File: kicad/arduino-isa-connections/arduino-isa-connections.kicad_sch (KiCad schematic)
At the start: 2 parts, among them J1 Trident TVGA9000i-1, X1 14.31818MHz

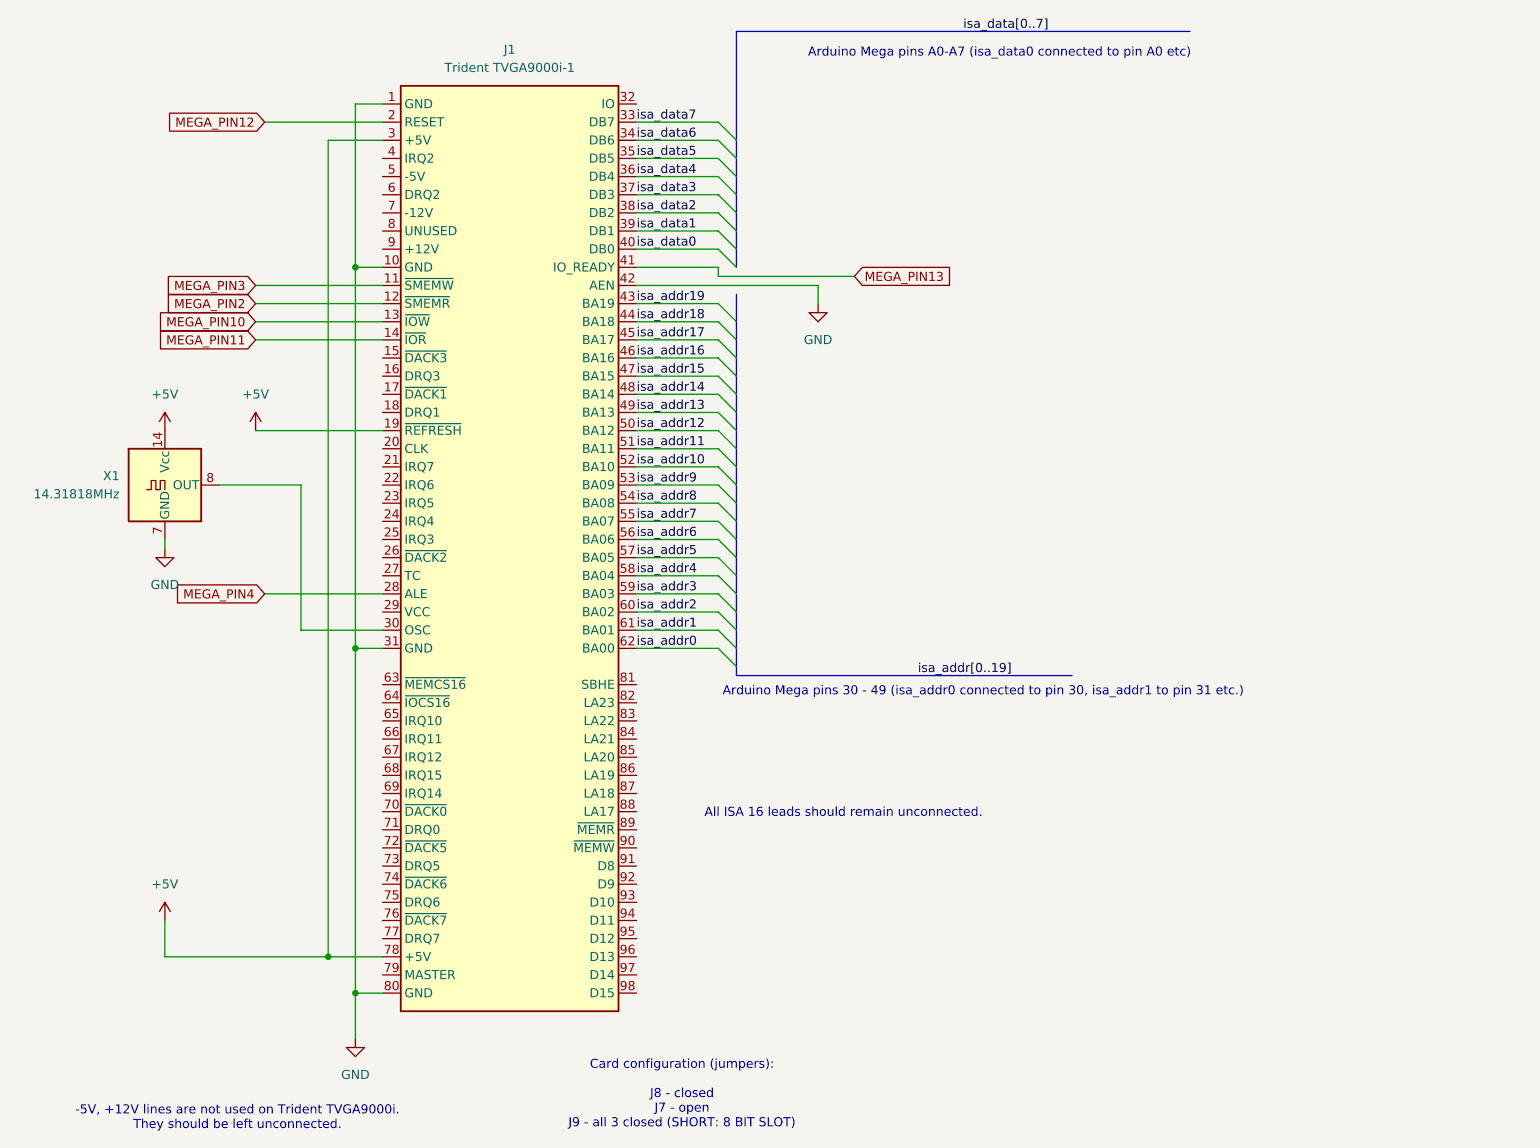
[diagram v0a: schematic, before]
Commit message: updated schematics
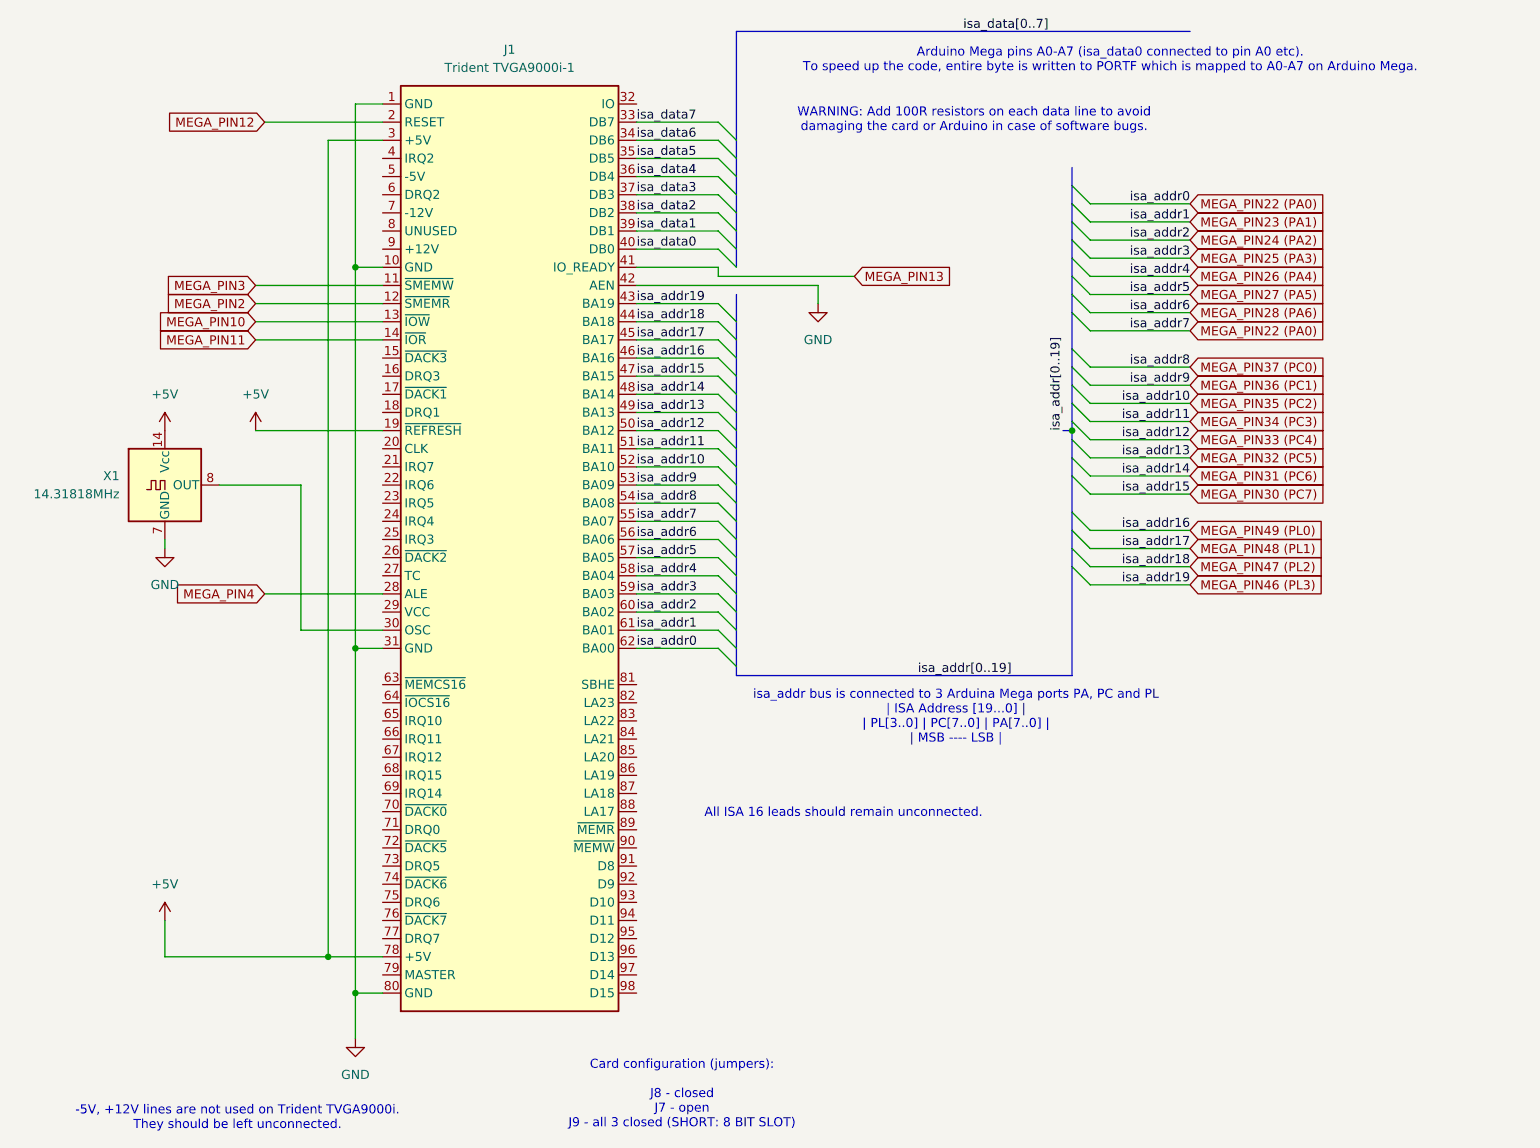
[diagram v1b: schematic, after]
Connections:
- net isa_addr7 is gone; now on net MEGA_PIN22 (PA0): J1.55 (BA07)
- net isa_addr0 renamed MEGA_PIN22 (PA0)
- net isa_addr1 renamed MEGA_PIN23 (PA1)
- net isa_addr10 renamed MEGA_PIN35 (PC2)
- net isa_addr11 renamed MEGA_PIN34 (PC3)
- net isa_addr12 renamed MEGA_PIN33 (PC4)
- net isa_addr13 renamed MEGA_PIN32 (PC5)
- net isa_addr14 renamed MEGA_PIN31 (PC6)
- net isa_addr15 renamed MEGA_PIN30 (PC7)
- net isa_addr16 renamed MEGA_PIN49 (PL0)
- net isa_addr17 renamed MEGA_PIN48 (PL1)
- net isa_addr18 renamed MEGA_PIN47 (PL2)
- net isa_addr19 renamed MEGA_PIN46 (PL3)
- net isa_addr2 renamed MEGA_PIN24 (PA2)
- net isa_addr3 renamed MEGA_PIN25 (PA3)
- net isa_addr4 renamed MEGA_PIN26 (PA4)
- net isa_addr5 renamed MEGA_PIN27 (PA5)
- net isa_addr6 renamed MEGA_PIN28 (PA6)
- net isa_addr8 renamed MEGA_PIN37 (PC0)
- net isa_addr9 renamed MEGA_PIN36 (PC1)
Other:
- note added: "Arduino Mega pins A0-A7 (isa_data0 connected to pin A0 etc). To speed up the code, entire byte is written to PORTF which is mapped to A0-A7 on Arduino Mega."
- note added: "WARNING: Add 100R resistors on each data line to avoid damaging the card or Arduino in case of software bugs."
- note added: "isa_addr bus is connected to 3 Arduina Mega ports PA, PC and PL | ISA Address [19...0] | | PL[3..0] | PC[7..0] | PA[7..0] | | MSB ---- LSB |"
- note removed: "Arduino Mega pins 30 - 49 (isa_addr0 connected to pin 30, isa_addr1 to pin 31 etc.)"
- note removed: "Arduino Mega pins A0-A7 (isa_data0 connected to pin A0 etc)"
